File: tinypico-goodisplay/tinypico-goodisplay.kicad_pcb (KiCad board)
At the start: 2 copper layers, 39.8 x 17.8 mm, 23 parts, among them Q1 Si1308, U1 TinypicoESP32_Symbol, U2 FPCConn

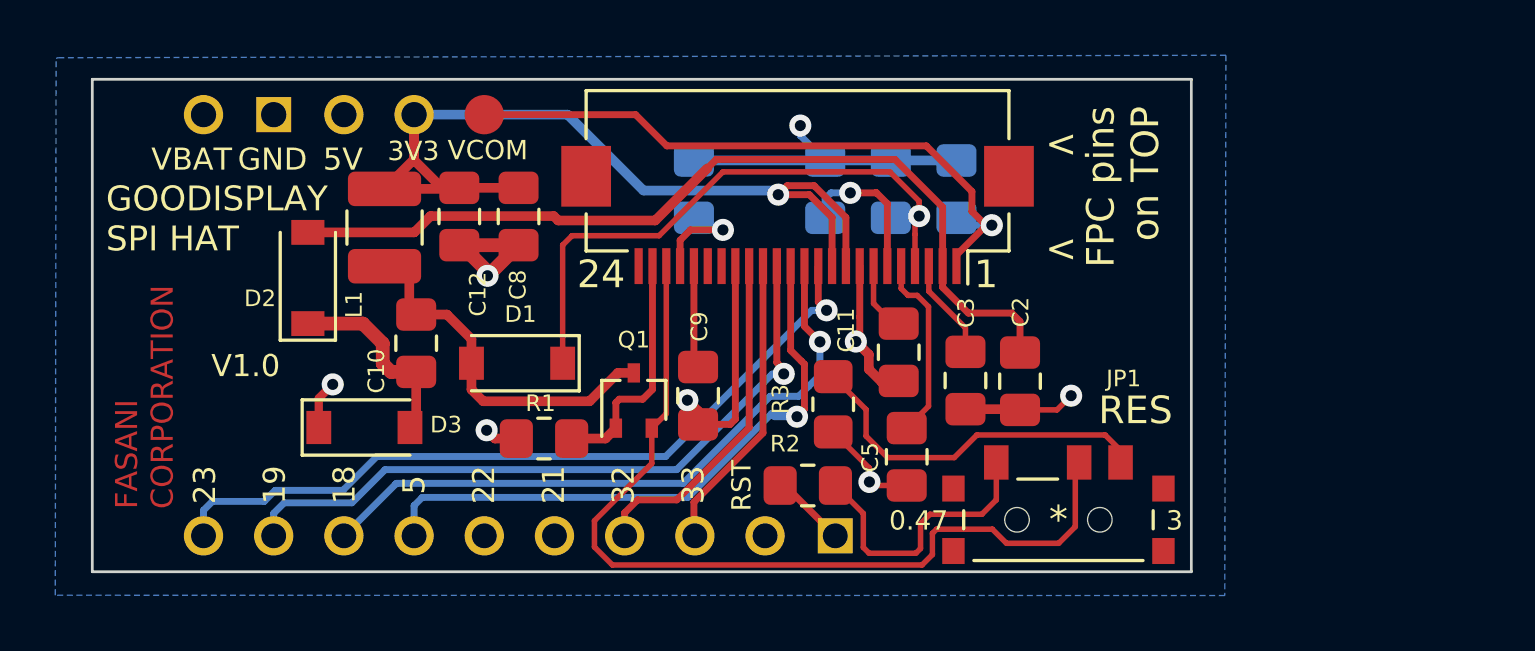
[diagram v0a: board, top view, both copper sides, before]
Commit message: Update tinypico adapter
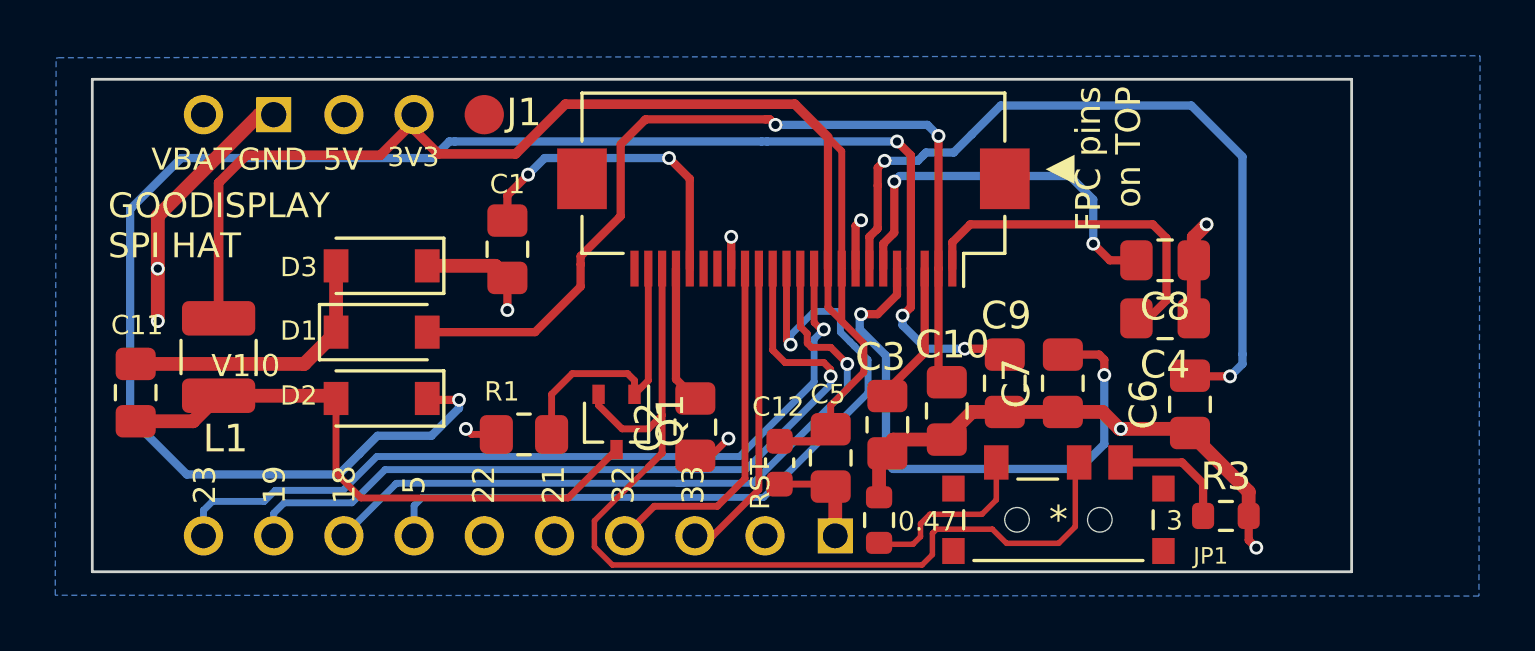
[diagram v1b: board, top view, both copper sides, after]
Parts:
- removed U2: FPCConn, footprint:Hirose_FH12-24S-0.5SH_1x24-1MP_P0.50mm_Horizontal
- added J1: FH12-24S-0.5SV55, footprint:Hirose_FH12-24S-0.5SH_1x24-1MP_P0.50mm_Horizontal, F.Cu at (97.6, 39.8)
- C1, C4, C6, C7: value 105 -> 1uF; moved to F.Cu
- C10: value 4.7uF50V -> 1uF
- C11: value 105 -> 4.7uF 50V
- C12: value 4.7uF50V -> 10uF50V; footprint Capacitor_SMD:C_0805_2012Metric_Pad1.18x1.45mm_HandSolder -> Capacitor_SMD:C_0603_1608Metric
- C2, C3, C5, C9: value 105 -> 1uF
- C8: value 104 -> 1uF
- R2, R3: footprint Resistor_SMD:R_0805_2012Metric_Pad1.20x1.40mm_HandSolder -> Resistor_SMD:R_0603_1608Metric
- moved C11 27.6 mm to (73.8, 46.1), turned to -90 degrees
- moved C8 23.4 mm to (111.0, 41.4), turned to 180 degrees
- moved C10 19.4 mm to (103.2, 46.8), turned to 90 degrees
- moved C1 16.4 mm to (87.2, 41.0), turned to 90 degrees
- moved C6 15.3 mm to (112.0, 46.6), turned to 90 degrees
- moved C7 15.1 mm to (107.3, 45.8), turned to 90 degrees
- moved R3 14.8 mm to (113.2, 50.6), turned to 0 degrees
- moved C12 14.6 mm to (97.1, 48.7)
- moved C2 11.9 mm to (94.0, 47.4)
- moved C9 11.1 mm to (105.2, 45.8)
- moved C4 11.0 mm to (111.0, 43.5), turned to 180 degrees
- moved L1 7.62 mm to (76.8, 44.9)
- moved D3 5.88 mm to (82.7, 41.5), turned to 180 degrees
- moved D2 5.11 mm to (82.7, 46.4), turned to 180 degrees
- moved D1 5.03 mm to (82.7, 44.0), turned to 0 degrees
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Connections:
- C1 pad 2: /VCOM -> Net-(C1-Pad2)
- C10 pad 1: Net-(C10-Pad1) -> GND
- C11 pad 1: GND -> Net-(C11-Pad1)
- C5 pad 2: Net-(C5-Pad2) -> +3V3
- C8 pad 2: +3V3 -> Net-(C8-Pad2)
- C9 pad 2: Net-(C9-Pad2) -> PREVGH
- D1 pad 1: Net-(C4-Pad2) -> Net-(C11-Pad1)
- D1 pad 2: Net-(C10-Pad1) -> Net-(C10-Pad2)
- D2 pad 1: Net-(C10-Pad2) -> PREVGH
- D2 pad 2: Net-(C2-Pad2) -> Net-(C11-Pad2)
- D3 pad 2: Net-(C10-Pad2) -> Net-(C11-Pad1)
- L1 pad 1: Net-(C10-Pad1) -> Net-(C11-Pad2)
- Q1 pad 3: Net-(C10-Pad1) -> Net-(C11-Pad2)
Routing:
- net PREVGH: track 0.00 -> 62.7 mm, vias 0 -> 4
- net Net-(C2-Pad2): track 32.3 -> 4.99 mm
- net Net-(C10-Pad2): track 7.18 -> 33.1 mm, vias 0 -> 2
- net /VCOM: track 24.0 -> 0.00 mm, vias 1 -> 0
- net Net-(C6-Pad2): track 5.46 -> 28.3 mm, vias 1 -> 2
- net Net-(C11-Pad2): track 2.45 -> 21.6 mm
- net Net-(C7-Pad2): track 3.87 -> 21.3 mm, vias 1 -> 2
- net +3V3: track 35.0 -> 50.2 mm, vias 1 -> 0
- net Net-(C8-Pad2): track 0.00 -> 14.4 mm, vias 0 -> 2
- net Net-(C10-Pad1): track 12.6 -> 0.00 mm
- net Net-(C1-Pad2): track 0.00 -> 11.6 mm, vias 0 -> 2
- net Net-(C11-Pad1): track 0.00 -> 10.1 mm
- net Net-(C4-Pad2): track 22.4 -> 12.8 mm, vias 1 -> 0
- net Net-(JP1-Pad3): track 13.2 -> 4.48 mm
- net Net-(C5-Pad2): track 6.79 -> 0.00 mm
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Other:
- board size 39.8 x 17.8 mm -> 45.6 x 17.8 mm
- board text added: "◀"
- board text removed: "1"
- board text removed: "24"
- board text removed: "<"
- board text removed: "FASANI CORPORATION"
- board text removed: "RES"
- board text removed: "VCOM"

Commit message: DRC
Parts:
- moved C12 2.08 mm to (97.2, 46.6)
- moved C2 0.39 mm to (94.0, 47.0)
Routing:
- net GND: track 45.7 -> 49.6 mm
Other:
- board text added: "V1.1"
- board text removed: "V1.0"

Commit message: #1 update SCH
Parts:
- J1: value FH12-24S-0.5SV55 -> AFC24-S24FIC-00; footprint footprint:Hirose_FH12-24S-0.5SH_1x24-1MP_P0.50mm_Horizontal -> footprint:AFC24-S24FIC-00
- L1: value 68uH1A -> 10uH; footprint Inductor_SMD:L_1210_3225Metric -> footprint:SWPA4030S1R0NT
- R1: footprint Resistor_SMD:R_0805_2012Metric_Pad1.20x1.40mm_HandSolder -> Resistor_SMD:R_0603_1608Metric
- moved J1 0.80 mm to (97.6, 39.0)
- moved L1 0.78 mm to (77.5, 45.0)
- moved R1 0.18 mm to (88.0, 47.5)
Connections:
- C4 pad 2: Net-(C4-Pad2) -> /VCOM
- J1 pad 1: Net-(C4-Pad2) -> /VCOM
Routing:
- net /VCOM: track 0.00 -> 35.0 mm
- net Net-(C4-Pad2): track 12.8 -> 0.00 mm
- net GND: track 49.6 -> 53.0 mm, vias 10 -> 11
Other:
- board size 45.6 x 17.8 mm -> 42.5 x 17.8 mm

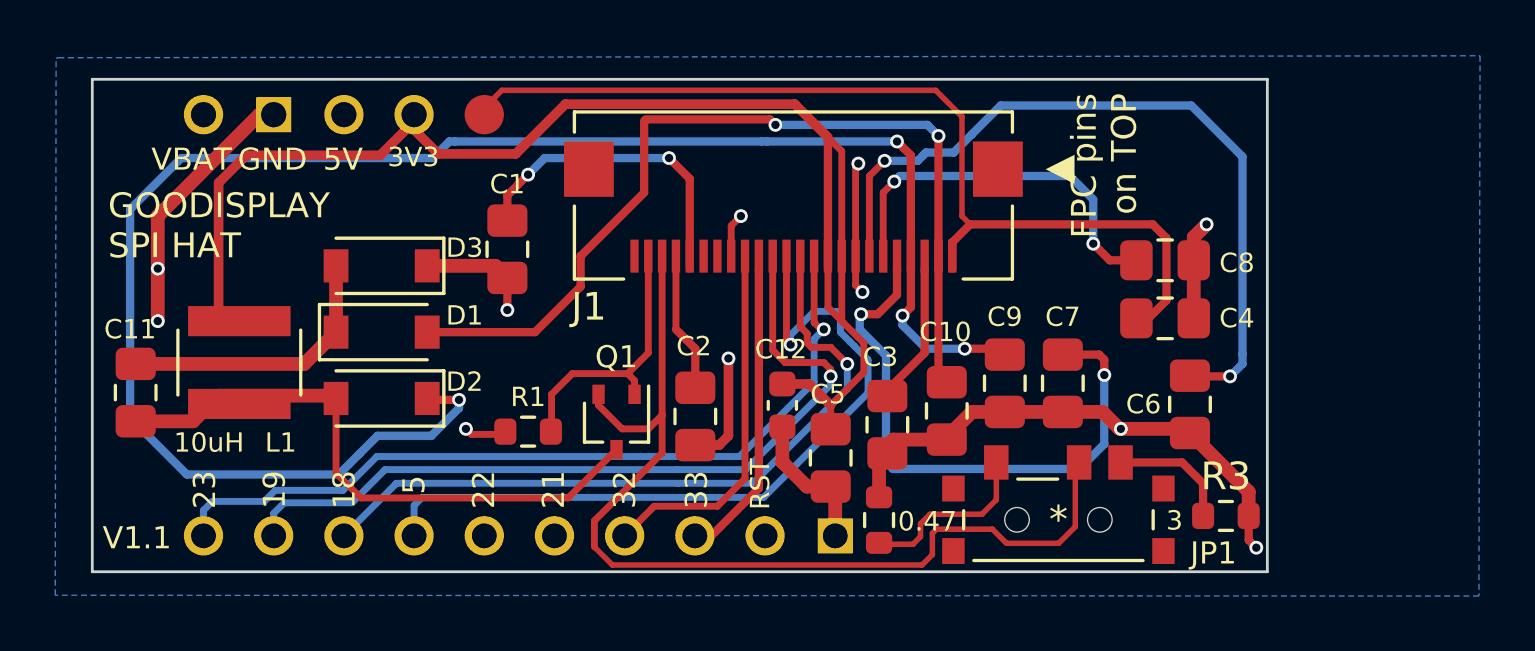
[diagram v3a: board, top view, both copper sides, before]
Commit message: Add optional EPD_RST pullup to 3V3
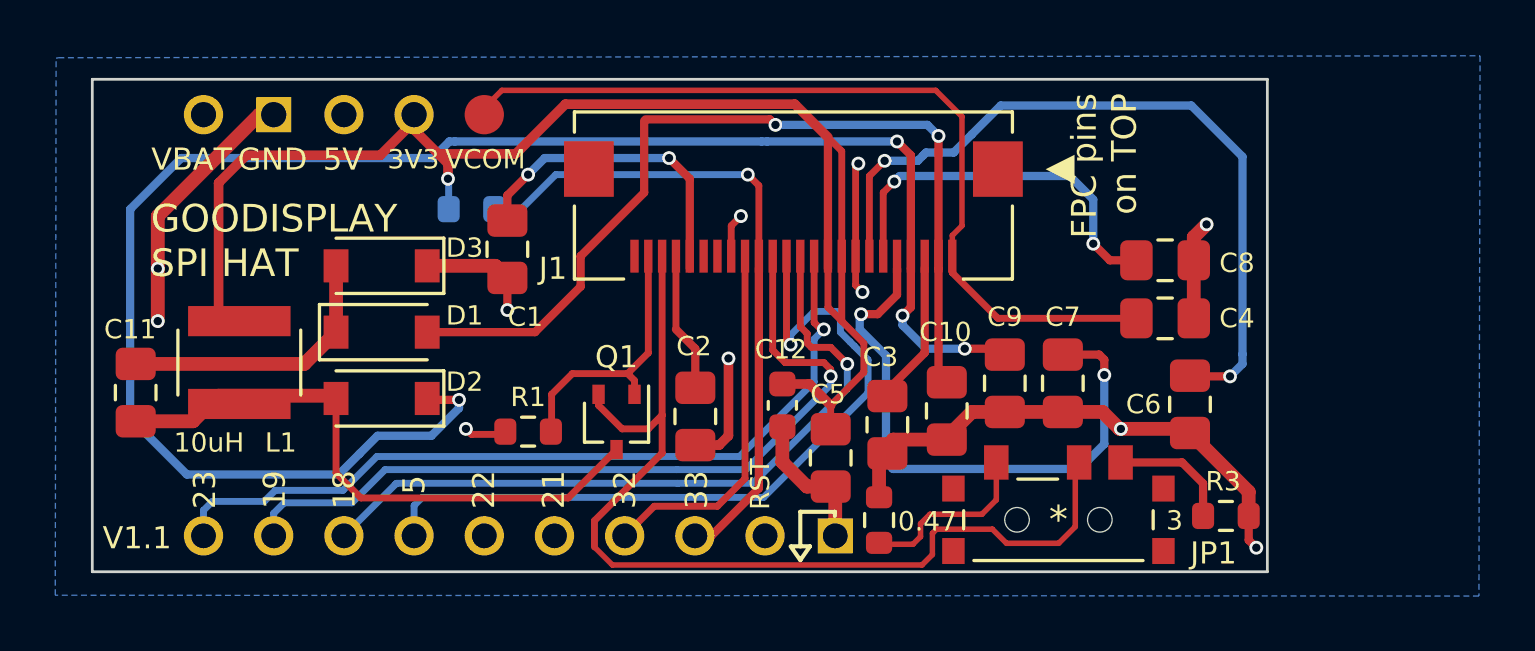
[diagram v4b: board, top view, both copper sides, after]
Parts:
- added R4: 10K, Resistor_SMD:R_0603_1608Metric, B.Cu at (86.0, 39.5)
- C1, C10, C2, C3, C7, C9: value 1uF -> 4.7uF
- C12: value 10uF50V -> 4.7uF
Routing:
- net /EPD_RST: track 11.0 -> 23.8 mm, vias 0 -> 1
- net /VCOM: track 35.0 -> 31.3 mm
- net +3V3: track 50.2 -> 52.4 mm, vias 0 -> 1
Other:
- board text added: "34"
- board text added: "35"
- board text added: "36"
- board text added: "37"
- board text added: "6"
- board text added: "7"
- board text added: "8"
- board text added: "9"
- board text added: "CORP."
- board text added: "Designed by:"
- board text added: "ESP32S3 tinypico IO▶"
- board text added: "FASANI"
- board text added: "Optional pull-up ▶ EPD_RST to 3V3"
- board text added: "VCOM"
